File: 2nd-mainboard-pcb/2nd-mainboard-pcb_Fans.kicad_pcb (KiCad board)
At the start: 2 copper layers, 51 parts, among them J11 Servo Motor SM, J12 Steckverbinder_Male_Fans, J15 Steckverbinder_Female_Motoren, J19 T2, J2 Fan_12/5V_Regelung, J20 T2, J21 T2, J22 T3, J3 FAN0, J4 FAN1, J5 FAN2, J6 FAN3, J7 Stepper Motor, J8 Servo Motor SM, J9 Microstepping, U12 MPU-6050, U7 TPM16050-S6TR, U8 RJK0456DPB-00-J5, U9 RJK0456DPB-00-J5

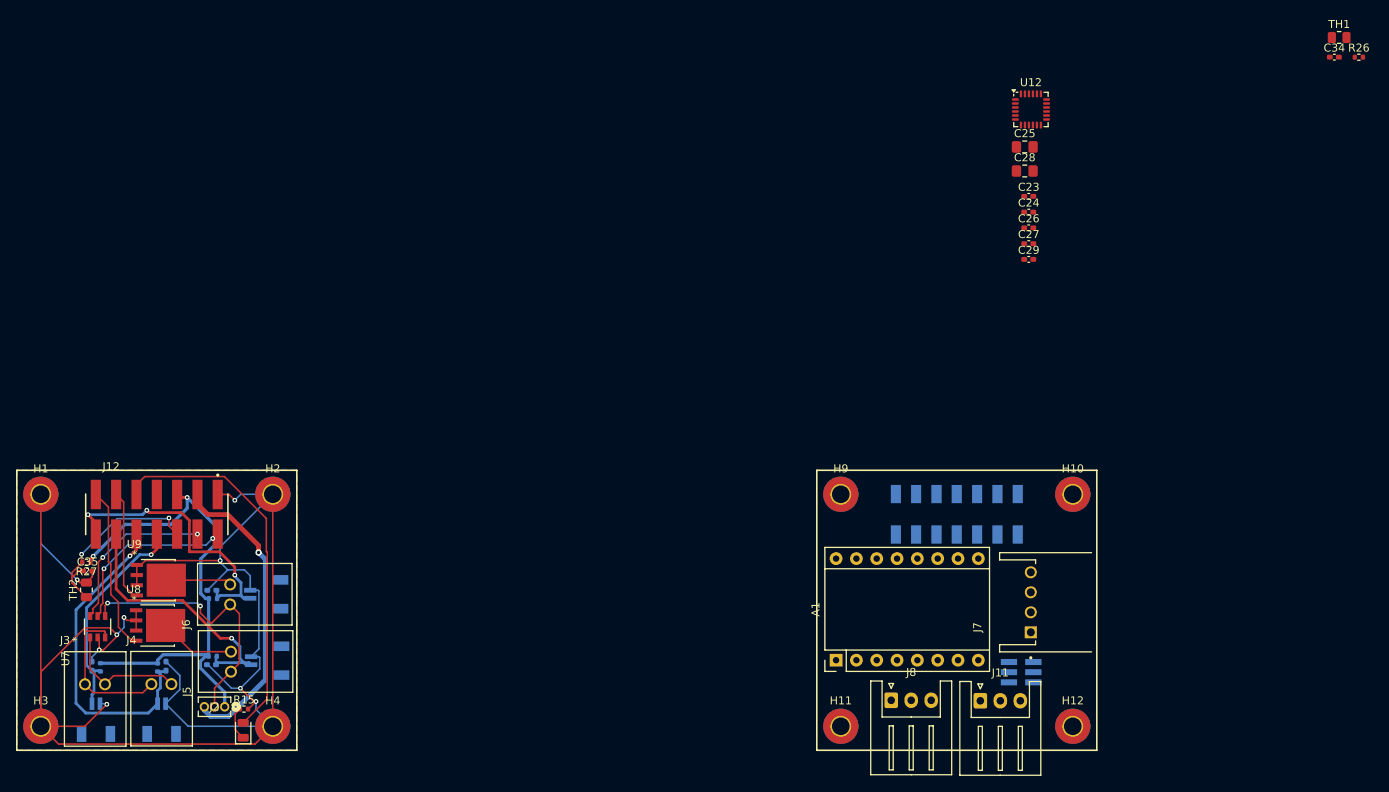
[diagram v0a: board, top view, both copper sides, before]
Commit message: pcb fans finished, pcb motors begin
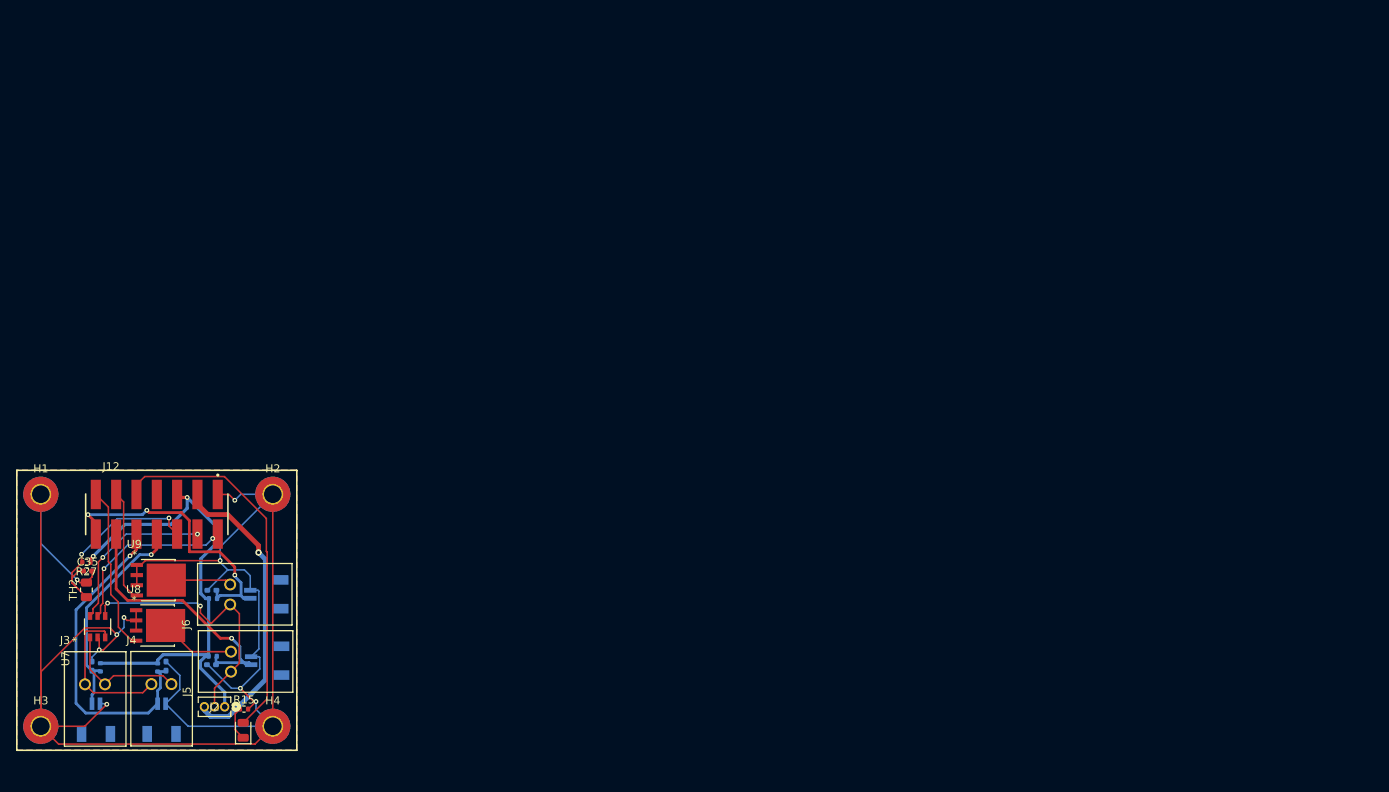
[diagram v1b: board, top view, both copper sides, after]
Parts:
- removed A1: Pololu_Breakout_DRV8825, Module:Pololu_Breakout-16_15.2x20.3mm
- removed C23, C24, C26, C27, C29: 100nF, Capacitor_SMD:C_0402_1005Metric_Pad0.74x0.62mm_HandSolder
- removed C25, C28: 4.7uF, Capacitor_SMD:C_0805_2012Metric_Pad1.18x1.45mm_HandSolder
- removed C34: 0.1µF, Capacitor_SMD:C_0402_1005Metric_Pad0.74x0.62mm_HandSolder
- removed H10, H11, H12, H9: MountHole, MountingHole:MountingHole_2.2mm_M2_Pad_TopBottom
- removed J11, J8: Servo Motor SM, Imported_Component_Footprints:JST_XH_S3B-XH-A_1x03_P2.50mm_Horizontal
- removed J15: Steckverbinder_Female_Motoren, Imported_Component_Footprints:SAMTEC_HLE-107-02-L-DV
- removed J7: Stepper Motor, Imported_Component_Footprints:JST_S4B-XH-A-1
- removed J9: Microstepping, Imported_Component_Footprints:FTSH-103-01-L-DH
- removed R26: 4k7, Resistor_SMD:R_0402_1005Metric
- removed TH1: Thermistor_NTC, Resistor_SMD:R_0805_2012Metric
- removed U12: MPU-6050, Sensor_Motion:InvenSense_QFN-24_4x4mm_P0.5mm
